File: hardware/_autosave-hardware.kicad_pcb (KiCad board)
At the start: 2 copper layers, 333.4 x 239.8 mm, 91 parts, among them J1 USB_C_Receptacle_USB2.0, J2 Conn_ST_STDC14, J3 Micro_SD_Card_Det, J4 RJHSE5380, J5 RJHSE5380, J6 OQ0271010000G, J7 OQ0271010000G, J8 Conn_02x13_Odd_Even_MountingP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, Q1 Si3129DV, Q2 PMDT290UNE, Q3 Si1967DH, SW1 218-8LPS, SW2 Boot0, SW3 User, SW4 nReset, U1 MAX17521, U2 AP2139AK-3.3, U3 USBLC6-4SC6, U4 TCAN1051HGV, U5 STM32G474VET6, Y1 25MHz

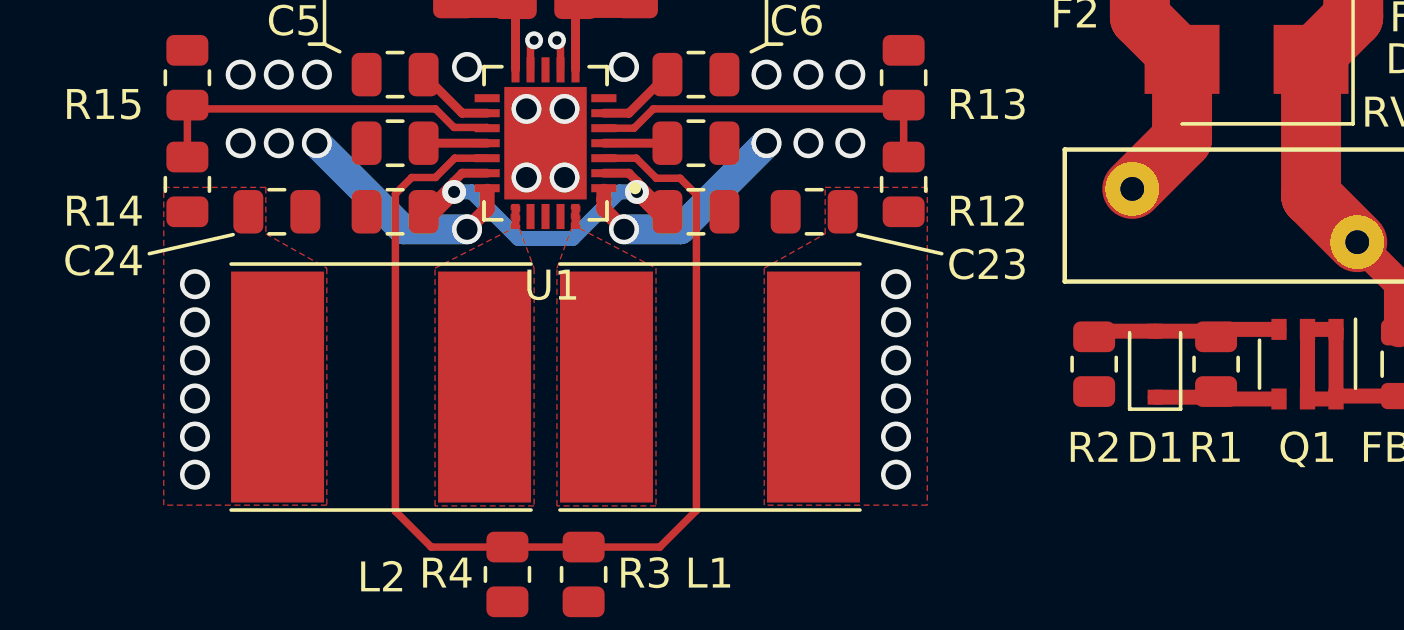
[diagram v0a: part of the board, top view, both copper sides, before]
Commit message: Power routing
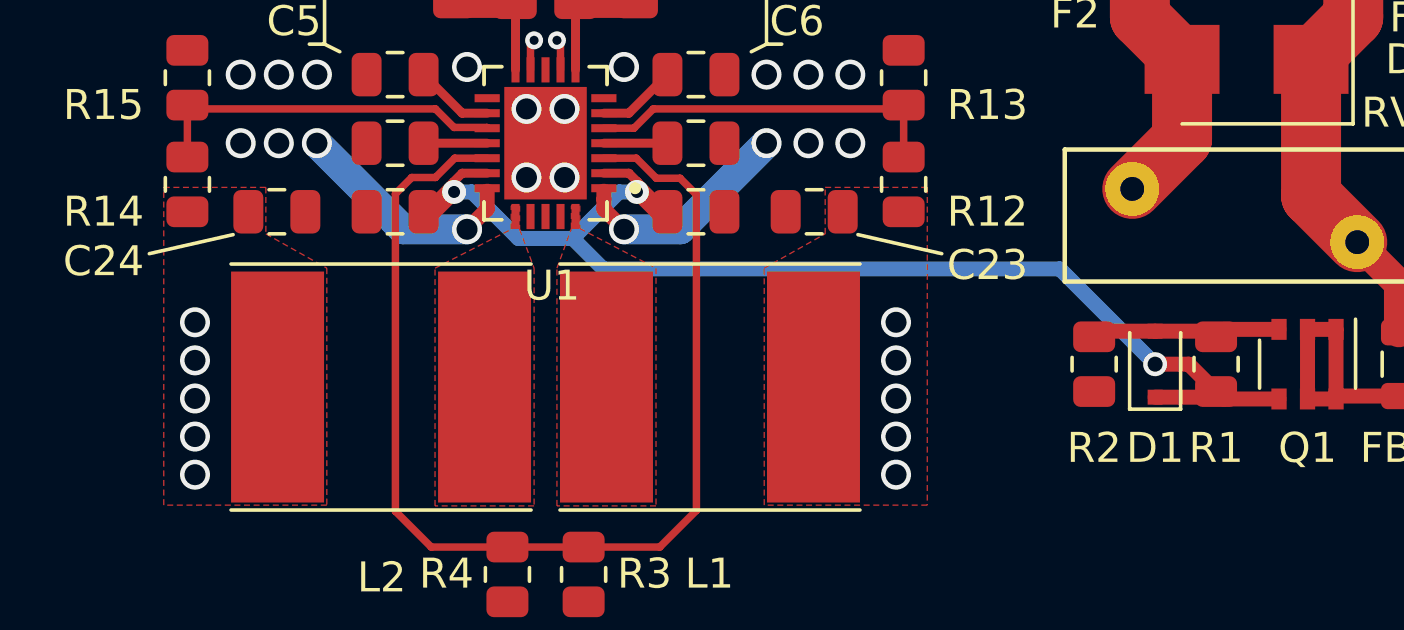
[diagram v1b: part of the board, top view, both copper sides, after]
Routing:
- net +24V: track 19.6 -> 43.1 mm, vias 2 -> 3
- net +5V: vias 6 -> 5
- net +3V3: vias 6 -> 5
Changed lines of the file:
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@@
     (thickness 1.6)
     (drawings 14)
-    (tracks 170)
+    (tracks 175)
     (zones 0)
     (modules 91)
@@
   )
   (setup
-    (last_trace_width 1)
+    (last_trace_width 0.5)
     (user_trace_width 0.3)
     (user_trace_width 0.5)
@@
   (via (at 71.628 148.1836) (size 0.8) (drill 0.4) (layers F.Cu B.Cu) (net 4))
   (via (at 65.532 148.1836) (size 0.8) (drill 0.4) (layers F.Cu B.Cu) (net 4))
-  (segment (start 91.1795 155.084) (end 90.932 154.8365) (width 0.5) (layer F.Cu) (net 4))
-  (segment (start 93.03 155.084) (end 91.1795 155.084) (width 0.5) (layer F.Cu) (net 4))
   (segment (start 90.7445 155.024) (end 90.932 154.8365) (width 0.5) (layer F.Cu) (net 4))
   (segment (start 88.9 155.024) (end 90.7445 155.024) (width 0.5) (layer F.Cu) (net 4))
@@
   (segment (start 71.034798 148.1836) (end 69.485398 149.733) (width 0.5) (layer B.Cu) (net 4))
   (segment (start 71.628 148.1836) (end 71.034798 148.1836) (width 0.5) (layer B.Cu) (net 4))
+  (segment (start 93.03 155.084) (end 91.1795 155.084) (width 0.5) (layer F.Cu) (net 4))
+  (segment (start 91.1795 155.084) (end 90.932 154.8365) (width 0.5) (layer F.Cu) (net 4))
+  (segment (start 90.0195 153.924) (end 90.932 154.8365) (width 0.5) (layer F.Cu) (net 4))
+  (segment (start 88.9 153.924) (end 88.9 153.924) (width 0.5) (layer F.Cu) (net 4))
+  (segment (start 88.9 153.924) (end 90.0195 153.924) (width 0.5) (layer F.Cu) (net 4))
+  (via (at 88.9 153.924) (size 0.8) (drill 0.5) (layers F.Cu B.Cu) (net 4))
+  (segment (start 88.9 153.924) (end 85.725 150.749) (width 0.5) (layer B.Cu) (net 4))
+  (segment (start 70.501398 150.749) (end 69.485398 149.733) (width 0.5) (layer B.Cu) (net 4))
+  (segment (start 85.725 150.749) (end 70.501398 150.749) (width 0.5) (layer B.Cu) (net 4))
   (via (at 56.896 157.607) (size 1) (drill 0.7) (layers F.Cu B.Cu) (net 5))
   (via (at 56.896 156.337) (size 1) (drill 0.7) (layers F.Cu B.Cu) (net 5))
@@
   (via (at 56.896 153.797) (size 1) (drill 0.7) (layers F.Cu B.Cu) (net 5))
   (via (at 56.896 152.527) (size 1) (drill 0.7) (layers F.Cu B.Cu) (net 5))
-  (via (at 56.896 151.257) (size 1) (drill 0.7) (layers F.Cu B.Cu) (net 5))
   (via (at 80.264 157.607) (size 1) (drill 0.7) (layers F.Cu B.Cu) (net 10))
   (via (at 80.264 156.337) (size 1) (drill 0.7) (layers F.Cu B.Cu) (net 10))
@@
   (via (at 80.264 153.797) (size 1) (drill 0.7) (layers F.Cu B.Cu) (net 10))
   (via (at 80.264 152.527) (size 1) (drill 0.7) (layers F.Cu B.Cu) (net 10))
-  (via (at 80.264 151.257) (size 1) (drill 0.7) (layers F.Cu B.Cu) (net 10))
   (segment (start 91.1795 152.764) (end 90.932 153.0115) (width 0.5) (layer F.Cu) (net 11))
   (segment (start 93.03 152.764) (end 91.1795 152.764) (width 0.5) (layer F.Cu) (net 11))
@@
   (segment (start 81.106 132.334) (end 76.28 127.508) (width 2) (layer F.Cu) (net 18))
   (segment (start 88.392 132.334) (end 81.106 132.334) (width 2) (layer F.Cu) (net 18))
-  (segment (start 95.0275 154.9865) (end 94.93 155.084) (width 0.5) (layer F.Cu) (net 20))
-  (segment (start 97.028 154.9865) (end 95.0275 154.9865) (width 0.5) (layer F.Cu) (net 20))
-  (segment (start 94.93 155.084) (end 94.93 152.764) (width 0.5) (layer F.Cu) (net 20))
   (segment (start 93.98 155.084) (end 93.98 152.764) (width 0.5) (layer F.Cu) (net 20))
-  (segment (start 94.93 155.084) (end 93.98 155.084) (width 0.5) (layer F.Cu) (net 20))
   (segment (start 94.93 152.764) (end 93.98 152.764) (width 0.5) (layer F.Cu) (net 20))
+  (segment (start 94.93 155.084) (end 94.93 152.764) (width 0.5) (layer F.Cu) (net 20))
+  (segment (start 94.93 155.084) (end 93.98 155.084) (width 0.5) (layer F.Cu) (net 20))
+  (segment (start 95.0275 154.9865) (end 94.93 155.084) (width 0.5) (layer F.Cu) (net 20))
+  (segment (start 97.028 154.9865) (end 95.0275 154.9865) (width 0.5) (layer F.Cu) (net 20))
   (segment (start 245.326 121.704) (end 244.856 122.174) (width 0.3) (layer F.Cu) (net 41))
   (segment (start 245.326 116.166) (end 245.326 121.704) (width 0.3) (layer F.Cu) (net 41))
@@
     (polygon
       (pts
-        (xy 75.946 147.574) (xy 73.279 150.241) (xy 70.993 150.241) (xy 68.199 150.241) (xy 68.834 149.733)
-        (xy 70.993 148.717) (xy 72.644 148.717) (xy 74.93 146.558)
+        (xy 75.946 147.574) (xy 73.279 150.241) (xy 68.453 150.241) (xy 68.453 149.479) (xy 69.469 149.479)
+        (xy 70.231 148.717) (xy 72.644 148.717) (xy 74.93 146.558)
       )
     )
@@
     (polygon
       (pts
-        (xy 64.135 148.717) (xy 66.167 148.717) (xy 68.326 149.733) (xy 68.58 150.241) (xy 66.294 150.241)
+        (xy 64.135 148.717) (xy 66.929 148.717) (xy 67.691 149.479) (xy 68.707 149.479) (xy 68.707 150.241)
         (xy 63.627 150.241) (xy 60.96 147.574) (xy 61.976 146.558)
       )
